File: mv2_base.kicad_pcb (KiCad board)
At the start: 4 copper layers, 69 x 64 mm, 55 parts, among them J1 Conn_01x20, J2 OLED, U1 TPS65130RGE

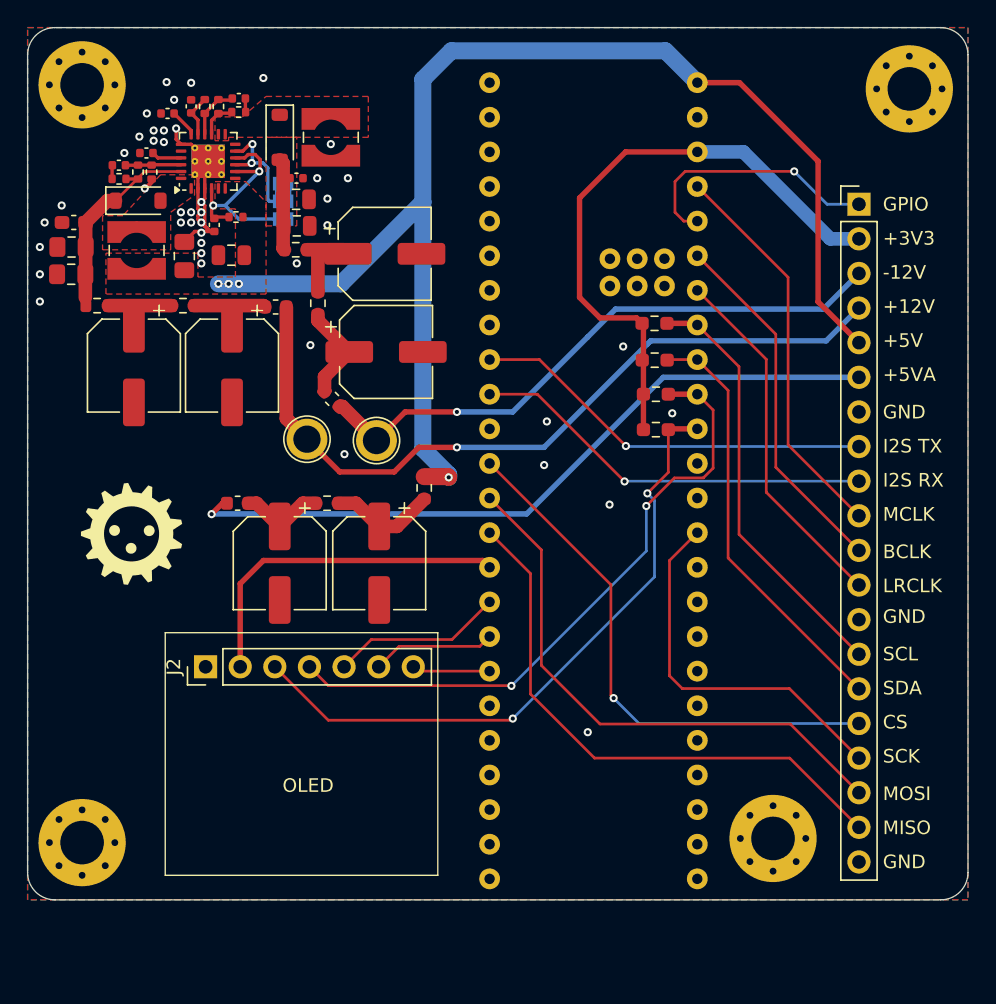
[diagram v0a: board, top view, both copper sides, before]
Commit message: Add jumpers in power rails and more test points
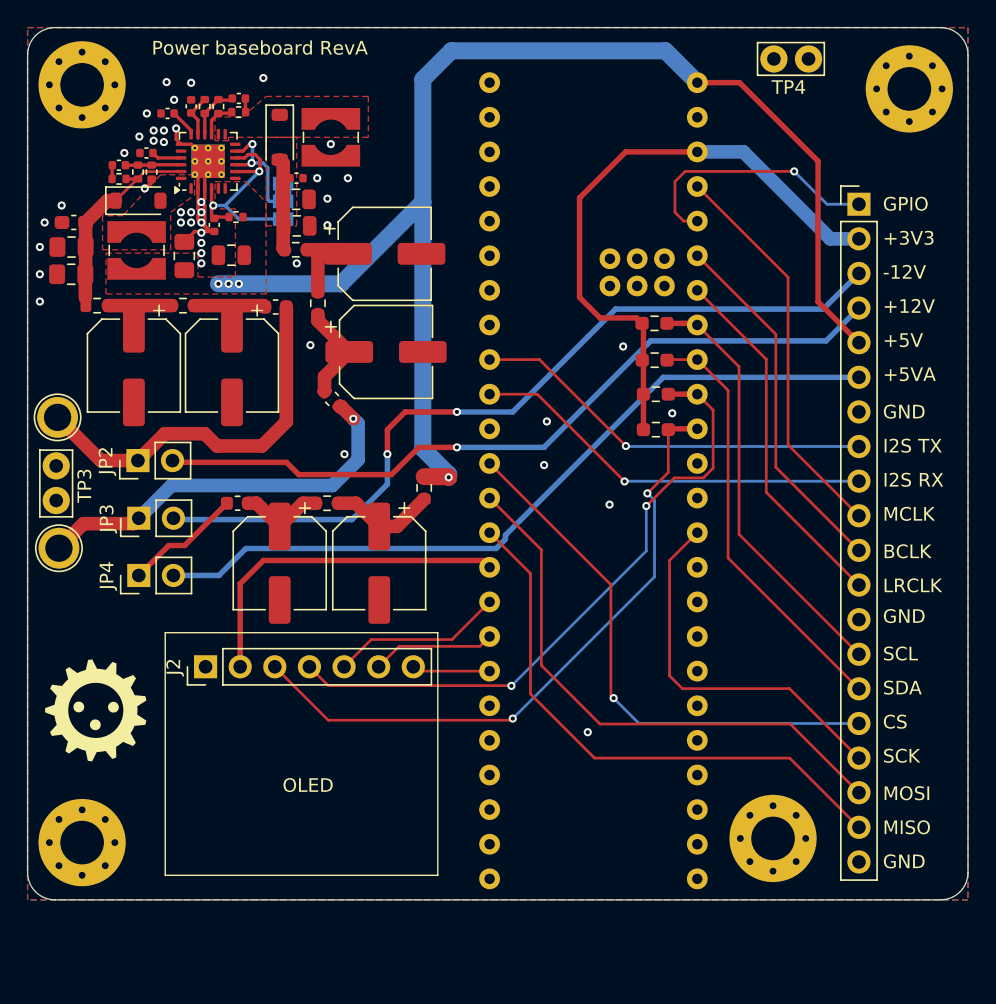
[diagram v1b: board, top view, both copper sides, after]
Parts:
- added JP2: Jumper_2_Open, Connector_PinHeader_2.54mm:PinHeader_1x02_P2.54mm_Vertical, F.Cu at (90.1, 97.0)
- added JP3: Jumper_2_Open, Connector_PinHeader_2.54mm:PinHeader_1x02_P2.54mm_Vertical, F.Cu at (90.2, 101.2)
- added JP4: Jumper_2_Open, Connector_PinHeader_2.54mm:PinHeader_1x02_P2.54mm_Vertical, F.Cu at (90.2, 105.4)
- added TP3: Groundpoint, TestPoint:TestPoint_Bridge_Pitch2.54mm_Drill1.0mm, F.Cu at (84.1, 99.9)
- added TP4: Groundpoint, TestPoint:TestPoint_Bridge_Pitch2.54mm_Drill1.0mm, F.Cu at (136.8, 67.5)
- moved TP2 24.6 mm to (84.3, 103.4)
- moved TP1 18.4 mm to (84.2, 93.8)
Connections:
- L3 pad 2: +12V -> Net-(JP2-A)
- L4 pad 2: -12V -> Net-(JP3-A)
- L5 pad 2: +5VA -> Net-(JP4-A)
- TP1 pad 1: +12V -> Net-(JP2-A)
- TP2 pad 1: -12V -> Net-(JP3-A)
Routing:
- net Net-(JP3-A): track 0.00 -> 29.2 mm, vias 0 -> 1
- net Net-(JP2-A): track 0.00 -> 28.4 mm
- net -12V: track 44.2 -> 60.2 mm, vias 1 -> 2
- net Net-(JP4-A): track 0.00 -> 8.66 mm
- net +5VA: track 53.1 -> 56.5 mm, vias 1 -> 0
- net +12V: track 56.8 -> 55.9 mm
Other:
- board text added: "Power baseboard RevA"

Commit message: New filters
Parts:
- removed C15, C16, C20, C22, C23, C24: 120uF, Capacitor_SMD:CP_Elec_6.3x7.7
- removed C19: 4.7uF, Capacitor_SMD:C_0805_2012Metric_Pad1.18x1.45mm_HandSolder
- removed JP4: Jumper_2_Open, Connector_PinHeader_2.54mm:PinHeader_1x02_P2.54mm_Vertical
- removed L3, L4: 600@100Mhz, Inductor_SMD:L_0603_1608Metric
- removed R12, R13, R14, R15: 3.4, Resistor_SMD:R_0603_1608Metric
- added C25: 22uF, Capacitor_SMD:C_0805_2012Metric, F.Cu at (86.0, 87.8)
- added C26: 22uF, Capacitor_SMD:C_0805_2012Metric, F.Cu at (92.4, 87.0)
- added C27: 22uF, Capacitor_SMD:C_0805_2012Metric, F.Cu at (98.6, 86.2)
- added C28: 22uF, Capacitor_SMD:C_0805_2012Metric, F.Cu at (105.6, 84.8)
- added C29: 22uF, Capacitor_SMD:C_0805_2012Metric, F.Cu at (98.2, 90.8)
- added C30: 22uF, Capacitor_SMD:C_0805_2012Metric, F.Cu at (99.0, 97.0)
- added D3: B5819W SL, Diode_SMD:D_SOD-123, F.Cu at (89.6, 90.0)
- added D4: B5819W SL, Diode_SMD:D_SOD-123, F.Cu at (102.8, 87.9)
- added D5: B5819W SL, Diode_SMD:D_SOD-123, F.Cu at (96.0, 94.4)
- added L6: 600@100Mhz, Inductor_SMD:L_0603_1608Metric, F.Cu at (101.6, 81.8)
- added L7: 600@100Mhz, Inductor_SMD:L_0603_1608Metric, F.Cu at (101.8, 94.2)
- added Q1: SS8550, Package_TO_SOT_SMD:SOT-23, F.Cu at (102.8, 84.8)
- added Q2: S8050, Package_TO_SOT_SMD:SOT-23, F.Cu at (89.5, 86.9)
- added Q3: S8050, Package_TO_SOT_SMD:SOT-23, F.Cu at (99.1, 94.2)
- added R18: 500, Resistor_SMD:R_0402_1005Metric, F.Cu at (100.2, 92.0)
- R16, R17: value 3.4 -> 500; footprint Resistor_SMD:R_0603_1608Metric -> Resistor_SMD:R_0402_1005Metric
- moved R16 27.7 mm to (86.5, 86.2), turned to 0 degrees
- moved L5 19.5 mm to (86.3, 84.1), turned to -90 degrees
- moved R17 16.5 mm to (100.4, 84.0), turned to 90 degrees
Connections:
- L5 pad 1: Net-(C16-Pad1) -> Net-(D1-K)
- L5 pad 2: Net-(JP4-A) -> Net-(Q2-C)
- R16 pad 1: +5V -> Net-(Q2-C)
- R16 pad 2: Net-(C15-Pad1) -> Net-(D3-K)
- R17 pad 1: Net-(C15-Pad1) -> Net-(D4-K)
- R17 pad 2: Net-(C16-Pad1) -> Net-(Q1-C)
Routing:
- net Net-(D4-A): track 29.2 -> 42.3 mm, vias 1 -> 4
- net Net-(JP4-A): track 8.66 -> 0.00 mm
- net Net-(C15-Pad1): track 7.83 -> 0.00 mm
- net Net-(C22-Pad1): track 7.34 -> 0.00 mm
- net Net-(D4-K): track 0.00 -> 6.86 mm
- net Net-(C16-Pad1): track 6.36 -> 0.00 mm
- net Net-(C20-Pad1): track 6.27 -> 0.00 mm
- net Net-(D3-A): track 28.4 -> 22.3 mm
- net Net-(D3-K): track 0.00 -> 5.48 mm
- net Net-(D5-K): track 0.00 -> 5.46 mm
- net Net-(Q2-C): track 0.00 -> 5.23 mm
- net Net-(C24-Pad1): track 5.23 -> 0.00 mm
- net Net-(C23-Pad1): track 4.65 -> 0.00 mm
- net Net-(Q1-C): track 0.00 -> 4.24 mm
- net Net-(Q3-C): track 0.00 -> 3.57 mm
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
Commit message: Implement +48V supply
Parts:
- added C13: 33nF, Capacitor_SMD:C_0603_1608Metric, F.Cu at (98.7, 112.2)
- added C14: 330pF, Capacitor_SMD:C_0603_1608Metric, F.Cu at (97.2, 112.2)
- added C15: 22nF, Capacitor_SMD:C_0402_1005Metric, F.Cu at (100.9, 109.7)
- added C16: 1uF, Capacitor_SMD:C_0402_1005Metric, F.Cu at (101.9, 103.3)
- added C17: 0.1uF, Capacitor_SMD:C_0402_1005Metric, F.Cu at (107.0, 104.5)
- added C18: 0.1uF, Capacitor_SMD:C_0402_1005Metric, F.Cu at (100.0, 103.3)
- added C19: 4.7uF, Capacitor_SMD:C_0805_2012Metric, F.Cu at (107.0, 103.0)
- added C20: 10uF, Capacitor_SMD:C_0805_2012Metric_Pad1.18x1.45mm_HandSolder, F.Cu at (105.6, 114.5)
- added D6: SS210, Diode_SMD:D_SMA, F.Cu at (107.2, 106.8)
- added L3: 4.7uH, Inductor_SMD:L_Wuerth_WE-TPC-3816, F.Cu at (105.0, 111.0)
- added L8: 600@100Mhz, Inductor_SMD:L_0603_1608Metric, F.Cu at (112.2, 111.0)
- added R12: 100k, Resistor_SMD:R_0402_1005Metric, F.Cu at (101.9, 109.7)
- added R13: 2.2k, Resistor_SMD:R_0402_1005Metric, F.Cu at (99.9, 109.7)
- added R14: 100k, Resistor_SMD:R_0402_1005Metric, F.Cu at (101.2, 112.8)
- added R15: 1.5k, Resistor_SMD:R_0402_1005Metric, F.Cu at (98.9, 109.7)
- added R19: 22k, Resistor_SMD:R_0402_1005Metric, F.Cu at (98.3, 104.6)
- added U3: LM5158, Package_DFN_QFN:WQFN-16-1EP_3x3mm_P0.5mm_EP1.68x1.68mm_ThermalVias, F.Cu at (101.1, 106.1)
- moved J2 7.41 mm to (95.4, 119.5)
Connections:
- net /VNEG renamed /12NREG
- net Net-(D1-K) renamed /12VREG
- J1 pad 1: /GPIO -> +48V
- U2 pad 22: /GPIO -> unconnected-(U2-Pad22)
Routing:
- net +48V: track 0.00 -> 101.9 mm, vias 0 -> 1
- net +5V: track 98.7 -> 146.9 mm, vias 6 -> 11
- net +3V3: track 70.4 -> 91.0 mm
- net /GPIO: track 19.0 -> 0.00 mm, vias 1 -> 0
- net /SCL1: track 47.6 -> 57.0 mm, vias 2 -> 1
- net /48VREG: track 0.00 -> 7.94 mm, vias 0 -> 16
- net /SDA1: track 46.8 -> 53.8 mm, vias 2 -> 1
- net /RESET: track 12.7 -> 19.5 mm
- net Net-(U3-FB): track 0.00 -> 6.32 mm, vias 0 -> 2
- net Net-(U3-COMP): track 0.00 -> 5.80 mm
- net /DC: track 9.06 -> 14.8 mm
- net /OLED_CS: track 5.73 -> 10.2 mm
- net Net-(D4-A): track 42.3 -> 40.4 mm
- net Net-(U3-MODE): track 0.00 -> 1.77 mm
- net -12V: track 59.1 -> 60.8 mm, vias 0 -> 1
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- added copper zone on B.Cu, net /48VREG
- added copper zone on F.Cu, net /48VREG
- added copper zone on In1.Cu, net /48VREG
- added copper zone on In2.Cu, net /48VREG
- added copper zone on F.Cu, net /SW
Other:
- board text added: "+48V"
- board text removed: "GPIO"

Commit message: Fix up some LCSC part numbers
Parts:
- R1: value 240k -> 200k
- R2: value 27k -> 24k
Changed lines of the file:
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@@
 			)
 		)
-		(property "LCSC" "C53987"
+		(property "LCSC" "C1538"
 			(at 0 0 180)
 			(unlocked yes)
@@
 			)
 		)
-		(property "LCSC" "C25741"
+		(property "LCSC" "C25879"
 			(at 0 0 90)
 			(unlocked yes)
@@
 			)
 		)
-		(property "LCSC" "C1653"
+		(property "LCSC" "C1555"
 			(at 0 0 0)
 			(unlocked yes)
@@
 			)
 		)
-		(property "LCSC" "C57112"
+		(property "LCSC" "C15195"
 			(at 0 0 180)
 			(unlocked yes)
@@
 			)
 		)
-		(property "LCSC" "C25803"
+		(property "LCSC" "C25741"
 			(at 0 0 90)
 			(unlocked yes)
@@
 			)
 		)
-		(property "LCSC" "C14663"
+		(property "LCSC" "C307331"
 			(at 0 0 0)
 			(unlocked yes)
@@
 			)
 		)
-		(property "LCSC" "C15850"
+		(property "LCSC" "C1779"
 			(at 0 0 0)
 			(unlocked yes)
@@
 			)
 		)
-		(property "LCSC" "C15850"
+		(property "LCSC" "C1779"
 			(at 0 0 180)
 			(unlocked yes)
@@
 			)
 		)
-		(property "LCSC" "C25879"
+		(property "LCSC" "C25741"
 			(at 0 0 90)
 			(unlocked yes)
@@
 			)
 		)
-		(property "LCSC" "C22775"
+		(property "LCSC" "C25076"
 			(at 0 0 180)
 			(unlocked yes)
@@
 			)
 		)
-		(property "LCSC" "C15850"
+		(property "LCSC" "C1779"
 			(at 0 0 0)
 			(unlocked yes)
@@
 			)
 		)
-		(property "LCSC" "C25879"
+		(property "LCSC" "C25741"
 			(at 0 0 0)
 			(unlocked yes)
@@
 			)
 		)
-		(property "LCSC" "C15850"
+		(property "LCSC" "C1779"
 			(at 0 0 180)
 			(unlocked yes)
@@
 			)
 		)
-		(property "Note" "Low ESR"
-			(at 0 0 180)
-			(unlocked yes)
-			(layer "F.Fab")
-			(hide yes)
-			(effects
-				(font
-					(size 1 1)
-					(thickness 0.15)
-				)
-			)
-		)
 		(property ki_fp_filters "C_*")
 		(sheetname "/")
@@
 			)
 		)
-		(property "Value" "240k"
+		(property "Value" "200k"
 			(at 0 1.17 90)
 			(layer "F.Fab")
@@
 			)
 		)
-		(property "LCSC" "C4197"
+		(property "LCSC" "C25768"
 			(at 0 0 270)
 			(unlocked yes)
@@
 			)
 		)
-		(property "Value" "27k"
+		(property "Value" "24k"
 			(at 0 1.17 90)
 			(layer "F.Fab")
@@
 			)
 		)
-		(property "LCSC" "C22967"
+		(property "LCSC" "C25764"
 			(at 0 0 90)
 			(unlocked yes)
@@
 			)
 		)
-		(property "LCSC" "C14663"
+		(property "LCSC" "C307331"
 			(at 0 0 180)
 			(unlocked yes)
@@
 			)
 		)
-		(property "LCSC" "C14663"
+		(property "LCSC" "C307331"
 			(at 0 0 270)
 			(unlocked yes)

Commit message: Fix up some LCSC part numbers
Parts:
- C8: value 7.5pF -> 10pF
- R2: value 24k -> 22k
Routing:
- net /12NREG: track 9.77 -> 16.0 mm, vias 0 -> 2
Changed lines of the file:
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@@
 			)
 		)
-		(property "Value" "7.5pF"
+		(property "Value" "10pF"
 			(at 0 1.16 180)
 			(layer "F.Fab")
@@
 			)
 		)
-		(property "LCSC" "C15850"
+		(property "LCSC" "C32949"
 			(at 0 0 180)
 			(unlocked yes)
@@
 			)
 		)
-		(property "LCSC" "C21120"
+		(property "LCSC" "C16772"
 			(at 0 0 90)
 			(unlocked yes)
@@
 			)
 		)
-		(property "LCSC" "C25768"
+		(property "LCSC" "C25764"
 			(at 0 0 270)
 			(unlocked yes)
@@
 			)
 		)
-		(property "Value" "24k"
+		(property "Value" "22k"
 			(at 0 1.17 90)
 			(layer "F.Fab")
@@
 			)
 		)
-		(property "LCSC" "C25764"
+		(property "LCSC" "C25768"
 			(at 0 0 90)
 			(unlocked yes)
@@
 	)
 	(segment
-		(start 100.5 74.9)
-		(end 100.75 75.15)
-		(width 1)
-		(layer "F.Cu")
-		(net 88)
-	)
-	(segment
 		(start 97 71.48)
 		(end 96.02 71.48)
@@
 	)
 	(segment
-		(start 96.02 71.48)
-		(end 96 71.5)
-		(width 0.25)
+		(start 100.5 74.9)
+		(end 100.75 75.15)
+		(width 1)
 		(layer "F.Cu")
 		(net 88)
@@
 	)
 	(segment
+		(start 96.02 71.48)
+		(end 96 71.5)
+		(width 0.25)
+		(layer "F.Cu")
+		(net 88)
+	)
+	(segment
 		(start 100.75 75.15)
 		(end 100.75 81.325)
@@
 		(net 88)
 	)
+	(via
+		(at 96.5 71.48)
+		(size 0.6)
+		(drill 0.3)
+		(layers "F.Cu" "B.Cu")
+		(net 88)
+	)
+	(via
+		(at 100.75 75.649998)
+		(size 0.6)
+		(drill 0.3)
+		(layers "F.Cu" "B.Cu")
+		(net 88)
+	)
+	(segment
+		(start 96.5 71.48)
+		(end 97.079943 71.48)
+		(width 0.2)
+		(layer "B.Cu")
+		(net 88)
+	)
+	(segment
+		(start 97.079943 71.48)
+		(end 100.75 75.150057)
+		(width 0.2)
+		(layer "B.Cu")
+		(net 88)
+	)
+	(segment
+		(start 100.75 75.150057)
+		(end 100.75 75.649998)
+		(width 0.2)
+		(layer "B.Cu")
+		(net 88)
+	)

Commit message: DRC fixes
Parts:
- moved C21 0.06 mm to (101.7, 79.8)
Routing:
- net /OUTN: track 0.00 -> 6.46 mm
- net +5V: track 146.9 -> 150.4 mm
- net /48VREG: track 7.94 -> 8.77 mm
- net GND: vias 107 -> 105
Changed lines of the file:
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@@
 	(footprint "Capacitor_SMD:C_0402_1005Metric"
 		(layer "F.Cu")
-		(at 88.7 75.3)
+		(at 88.7 75.28)
 		(descr "Capacitor SMD 0402 (1005 Metric), square (rectangular) end terminal, IPC_7351 nominal, (Body size source: IPC-SM-782 page 76, https://www.pcb-3d.com/wordpress/wp-content/uploads/ipc-sm-782a_amendment_1_and_2.pdf), generated with kicad-footprint-generator")
 		(tags "capacitor")
@@
 		(tags "Through hole pin header THT 1x07 2.54mm single row")
 		(property "Reference" "J2"
-			(at 0 -2.33 270)
+			(at -2.86 -1.33 270)
 			(layer "F.SilkS")
 			(effects
@@
 		(tags "capacitor")
 		(property "Reference" "C29"
-			(at 0 -1.68 90)
+			(at 0.3325 -1.82 90)
 			(layer "F.SilkS")
 			(effects
@@
 		(tags "capacitor")
 		(property "Reference" "C26"
-			(at 0 -1.68 90)
+			(at 0.2 2.48 90)
 			(layer "F.SilkS")
 			(effects
@@
 		(tags "resistor")
 		(property "Reference" "R16"
-			(at 0 -1.17 0)
+			(at -1.97 -0.04 0)
 			(layer "F.SilkS")
 			(effects
 				(font
-					(size 1 1)
+					(size 0.7 0.7)
 					(thickness 0.15)
 				)
@@
 		(tags "resistor")
 		(property "Reference" "R18"
-			(at 0 -1.17 0)
+			(at -2.41 0.2825 0)
 			(layer "F.SilkS")
 			(effects
@@
 		(tags "SOD-123")
 		(property "Reference" "D3"
-			(at 0 -2 0)
+			(at -0.355 1.89 0)
 			(layer "F.SilkS")
 			(effects
@@
 	(footprint "Capacitor_SMD:C_0805_2012Metric"
 		(layer "F.Cu")
-		(at 101.75 79.75)
+		(at 101.69 79.77)
 		(descr "Capacitor SMD 0805 (2012 Metric), square (rectangular) end terminal, IPC_7351 nominal, (Body size source: IPC-SM-782 page 76, https://www.pcb-3d.com/wordpress/wp-content/uploads/ipc-sm-782a_amendment_1_and_2.pdf, https://docs.google.com/spreadsheets/d/1BsfQQcO9C6DZCsRaXUlFlo91Tg2WpOkGARC1WS5S8t0/edit?usp=sharing), generated with kicad-footprint-generator")
 		(tags "capacitor")
@@
 	(footprint "Resistor_SMD:R_0402_1005Metric"
 		(layer "F.Cu")
-		(at 88.709999 76.3 180)
+		(at 88.709999 76.27 180)
 		(descr "Resistor SMD 0402 (1005 Metric), square (rectangular) end terminal, IPC_7351 nominal, (Body size source: IPC-SM-782 page 72, https://www.pcb-3d.com/wordpress/wp-content/uploads/ipc-sm-782a_amendment_1_and_2.pdf), generated with kicad-footprint-generator")
 		(tags "resistor")
@@
 		(tags "SOT TO_SOT_SMD")
 		(property "Reference" "Q2"
-			(at 0 -2.4 90)
+			(at -2.8325 3.37 90)
 			(layer "F.SilkS")
 			(effects
@@
 		(tags "resistor")
 		(property "Reference" "R17"
-			(at 0 -1.17 90)
+			(at 0.02381 -1.09 90)
 			(layer "F.SilkS")
 			(effects
 				(font
-					(size 1 1)
+					(size 0.7 0.7)
 					(thickness 0.15)
 				)
@@
 		(tags "SOT TO_SOT_SMD")
 		(property "Reference" "Q1"
-			(at 0 -2.4 90)
+			(at 2.84 2.92 90)
 			(layer "F.SilkS")
 			(effects
@@
 		(tags "capacitor")
 		(property "Reference" "C25"
-			(at 0 -1.68 0)
+			(at 0.57 -1.87 0)
 			(layer "F.SilkS")
 			(effects
@@
 		(tags "capacitor")
 		(property "Reference" "C30"
-			(at 0 -1.68 0)
+			(at -1.02 1.7975 0)
 			(layer "F.SilkS")
 			(effects
@@
 		(tags "SOD-123")
 		(property "Reference" "D5"
-			(at 0 -2 90)
+			(at -0.355 1.74 90)
 			(layer "F.SilkS")
 			(effects
@@
 		(tags "SOD-123")
 		(property "Reference" "D4"
-			(at 0 -2 0)
+			(at -0.08 1.9375 0)
 			(layer "F.SilkS")
 			(effects
@@
 		(tags "capacitor")
 		(property "Reference" "C27"
-			(at 0 -1.68 0)
+			(at 0 1.86 0)
 			(layer "F.SilkS")
 			(effects
@@
 		(tags "inductor")
 		(property "Reference" "L7"
-			(at 0 -1.43 90)
+			(at 0.7725 1.53 90)
 			(layer "F.SilkS")
 			(effects
@@
 		(tags "inductor")
 		(property "Reference" "L6"
-			(at 0 -1.43 0)
+			(at 2.38 0.09 0)
 			(layer "F.SilkS")
 			(effects
@@
 		(tags "inductor")
 		(property "Reference" "L5"
-			(at 0 -1.43 90)
+			(at -0.162779 1.552499 90)
 			(layer "F.SilkS")
 			(effects
@@
 		(tags "SOT TO_SOT_SMD")
 		(property "Reference" "Q3"
-			(at 0 -2.4 0)
+			(at 3.6975 2.4375 0)
 			(layer "F.SilkS")
 			(effects
@@
 		)
 		(fp_text user "3"
-			(at 2.600001 0 90)
+			(at 2.89 0.07 90)
 			(layer "B.SilkS")
 			(effects
@@
 	)
 	(segment
+		(start 96 77)
+		(end 96 77.6)
+		(width 0.25)
+		(layer "F.Cu")
+		(net 1)
+	)
+	(segment
 		(start 109 91)
 		(end 105 95)
@@
 	)
 	(segment
+		(start 97.6 78.1)
+		(end 97.8 78.3)
+		(width 0.25)
+		(layer "F.Cu")
+		(net 1)
+	)
+	(segment
+		(start 97.8 78.3)
+		(end 97.8 79.1)
+		(width 0.25)
+		(layer "F.Cu")
+		(net 1)
+	)
+	(segment
 		(start 134.24 69.24)
 		(end 131.14 69.24)
@@
 	)
 	(segment
+		(start 96.5 78.1)
+		(end 97.6 78.1)
+		(width 0.25)
+		(layer "F.Cu")
+		(net 1)
+	)
+	(segment
 		(start 100.51 103.35)
 		(end 100.87 103.71)
@@
 		(net 1)
 	)
+	(segment
+		(start 96 77.6)
+		(end 96.5 78.1)
+		(width 0.25)
+		(layer "F.Cu")
+		(net 1)
+	)
 	(via
 		(at 97.75 105.75)
@@
 	)
 	(via
-		(at 107 83.8)
+		(at 107.4 83.8)
 		(size 0.6)
 		(drill 0.3)
@@
 	)
 	(via
-		(at 104 83.8)
-		(size 0.6)
-		(drill 0.3)
-		(layers "F.Cu" "B.Cu")
-		(free yes)
-		(net 2)
-	)
-	(via
 		(at 104 79.7)
 		(size 0.6)
@@
 	)
 	(via
-		(at 105.6 82.6)
-		(size 0.6)
-		(drill 0.3)
-		(layers "F.Cu" "B.Cu")
-		(free yes)
-		(net 2)
-	)
-	(via
 		(at 102.5 104.65)
 		(size 0.6)
@@
 	)
 	(segment
-		(start 89.18 75.3)
-		(end 90.090001 75.3)
+		(start 89.18 75.28)
+		(end 89.2 75.3)
 		(width 0.25)
 		(layer "F.Cu")
@@
 	)
 	(segment
+		(start 93.2625 75.2625)
+		(end 90.9325 75.2625)
+		(width 0.25)
+		(layer "F.Cu")
+		(net 4)
+	)
+	(segment
 		(start 90.090001 75.3)
 		(end 90.1 75.290001)
@@
 	)
 	(segment
-		(start 93.2625 75.2625)
-		(end 90.9325 75.2625)
+		(start 89.2 75.3)
+		(end 90.090001 75.3)
 		(width 0.25)
 		(layer "F.Cu")
@@
 	)
 	(segment
+		(start 96.5 73.025)
+		(end 96.5 72.312)
+		(width 0.25)
+		(layer "F.Cu")
+		(net 12)
+	)
+	(segment
+		(start 96.759298 72.106)
+		(end 96.765298 72.1)
+		(width 0.25)
+		(layer "F.Cu")
+		(net 12)
+	)
+	(segment
+		(start 96 73.025)
+		(end 96 72.4)
+		(width 0.25)
+		(layer "F.Cu")
+		(net 12)
+	)
+	(segment
+		(start 96.706 72.106)
+		(end 96.759298 72.106)
+		(width 0.25)
+		(layer "F.Cu")
+		(net 12)
+	)
+	(segment
+		(start 96.5 72.312)
+		(end 96.706 72.106)
+		(width 0.25)
+		(layer "F.Cu")
+		(net 12)
+	)
+	(segment
+		(start 100 72.1)
+		(end 100.5 71.6)
+		(width 0.25)
+		(layer "F.Cu")
+		(net 12)
+	)
+	(segment
+		(start 96.294 72.106)
+		(end 96.706 72.106)
+		(width 0.25)
+		(layer "F.Cu")
+		(net 12)
+	)
+	(segment
+		(start 96.765298 72.1)
+		(end 100 72.1)
+		(width 0.25)
+		(layer "F.Cu")
+		(net 12)
+	)
+	(segment
+		(start 96 72.4)
+		(end 96.294 72.106)
+		(width 0.25)
+		(layer "F.Cu")
+		(net 12)
+	)
+	(segment
 		(start 134.2 102.38)
 		(end 134.2 90.08)
@@
 	)
 	(segment
-		(start 88.2 76.3)
+		(start 88.2 76.27)
 		(end 88.2 75.32)
 		(width 0.25)
@@
 	)
 	(segment
+		(start 88.22 75.3)
+		(end 88.22 75.28)
+		(width 0.25)
+		(layer "F.Cu")
+		(net 61)
+	)
+	(segment
 		(start 97.98 70.4)
 		(end 97.98 71.380001)
@@
 	)
 	(segment
-		(start 87.85 77.9)
-		(end 88.45 77.9)
-		(width 1)
+		(start 89.219998 76.3)
+		(end 89.219998 76.27)
+		(width 0.25)
 		(layer "F.Cu")
 		(net 83)
 	)
 	(segment
-		(start 89.229997 76.309999)
-		(end 89.219998 76.3)
-		(width 0.25)
+		(start 87.85 77.9)
+		(end 88.45 77.9)
+		(width 1)
 		(layer "F.Cu")
 		(net 83)
@@
 	)
 	(segment
-		(start 86.25 79.5)
-		(end 87.85 77.9)
-		(width 1)
+		(start 89.229997 76.309999)
+		(end 89.219998 76.3)
+		(width 0.25)
 		(layer "F.Cu")
 		(net 83)
 	)
 	(segment
-		(start 90.1 76.309999)
-		(end 89.229997 76.309999)
-		(width 0.25)
+		(start 86.25 79.5)
+		(end 87.85 77.9)
+		(width 1)
 		(layer "F.Cu")
 		(net 83)
@@
 	)
 	(segment
+		(start 90.1 76.309999)
+		(end 89.229997 76.309999)
+		(width 0.25)
+		(layer "F.Cu")
+		(net 83)
+	)
+	(segment
 		(start 97 71.48)
 		(end 96.02 71.48)
@@
 	)
 	(segment
-		(start 101.732376 112.082244)
-		(end 103.167756 112.082244)
+		(start 103.167756 112.082244)
+		(end 106.25 109)
 		(width 0.2)
 		(layer "B.Cu")
@@
 	)
 	(segment
-		(start 103.167756 112.082244)
-		(end 107.25 108)
+		(start 106.25 109)
+		(end 108.5 109)
+		(width 0.2)
+		(layer "B.Cu")
+		(net 89)
+	)
+	(segment
+		(start 101.732376 112.082244)
+		(end 103.167756 112.082244)
 		(width 0.2)
 		(layer "B.Cu")
